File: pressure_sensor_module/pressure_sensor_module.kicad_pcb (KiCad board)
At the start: 4 copper layers, 29 x 29.5 mm, 7 parts, among them J1 Conn_02x04_Odd_Even, J2 Conn_02x07_Odd_Even, U1 MPX5100AP

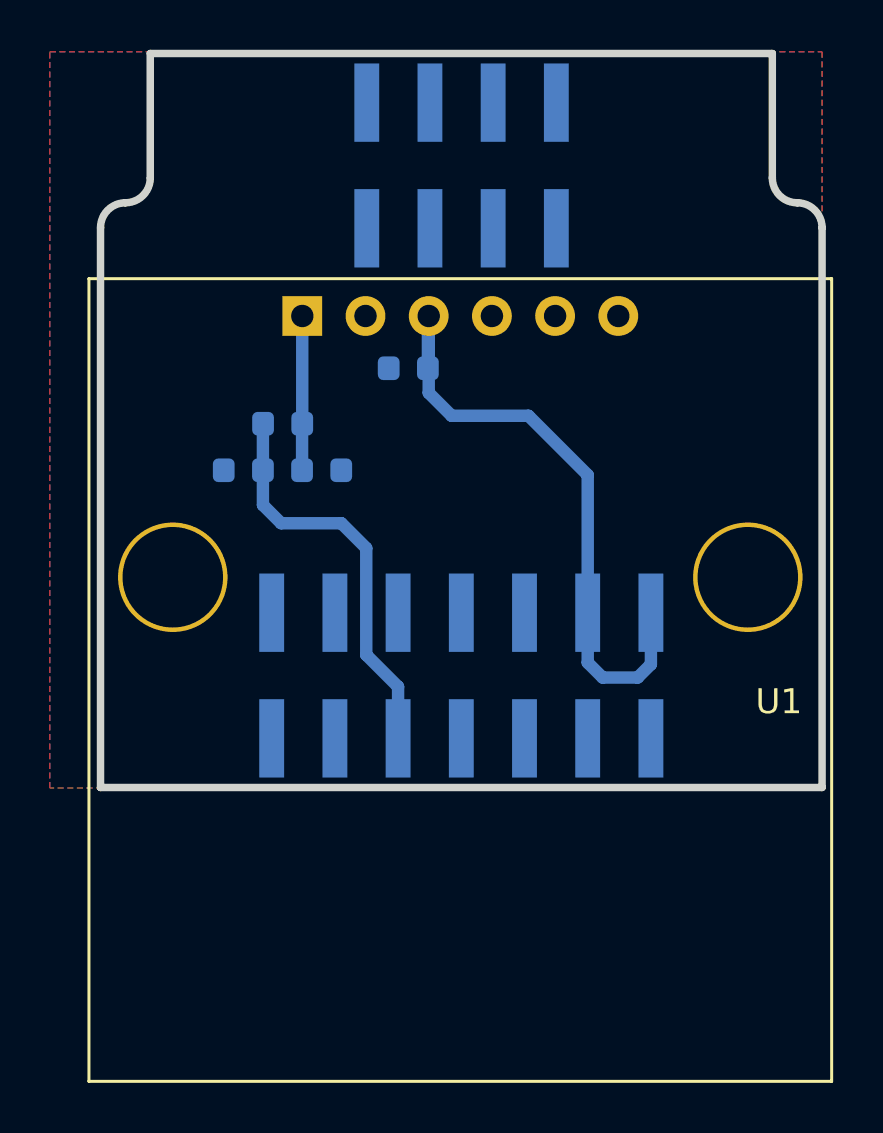
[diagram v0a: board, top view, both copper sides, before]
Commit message: added an LM358 to improve possible problems with impedance between the sensor and the STM
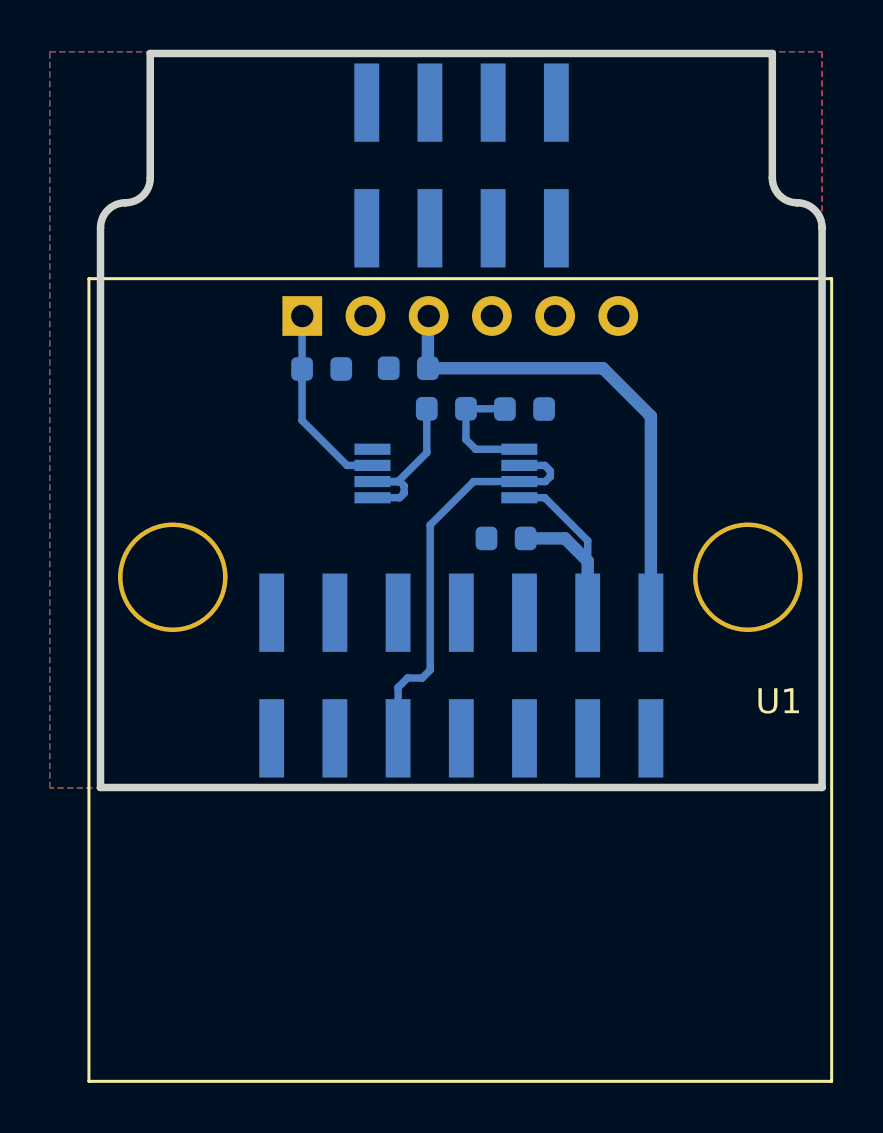
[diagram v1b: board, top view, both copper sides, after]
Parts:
- added C3: 1u, Capacitor_SMD:C_0603_1608Metric, B.Cu at (114.8, 49.6)
- added U2: LM358, Package_SO:TSSOP-8_4.4x3mm_P0.65mm, B.Cu at (112.3, 47.0)
- moved R2 11.6 mm to (115.5, 44.4), turned to 0 degrees
- moved R1 6.61 mm to (112.3, 44.4), turned to 180 degrees
- moved C2 4.07 mm to (107.3, 42.8)
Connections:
- R1 pad 1: /Analog -> Net-(R1-Pad1)
- R1 pad 2: Net-(C2-Pad1) -> Net-(R1-Pad2)
- R2 pad 1: /Analog -> Net-(R1-Pad1)
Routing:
- net Net-(R1-Pad2): track 0.00 -> 7.42 mm
- net +5V: track 25.6 -> 31.1 mm
- net Net-(R1-Pad1): track 0.00 -> 5.11 mm
- net Net-(C2-Pad1): track 6.20 -> 7.78 mm

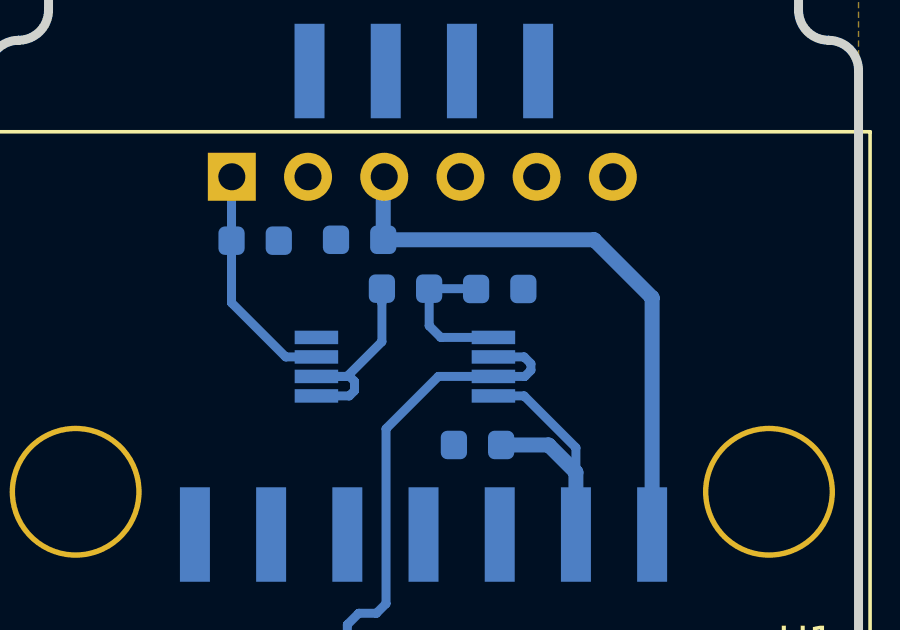
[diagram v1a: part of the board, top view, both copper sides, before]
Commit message: Added all references on silkscreen added BOM for sensor modules
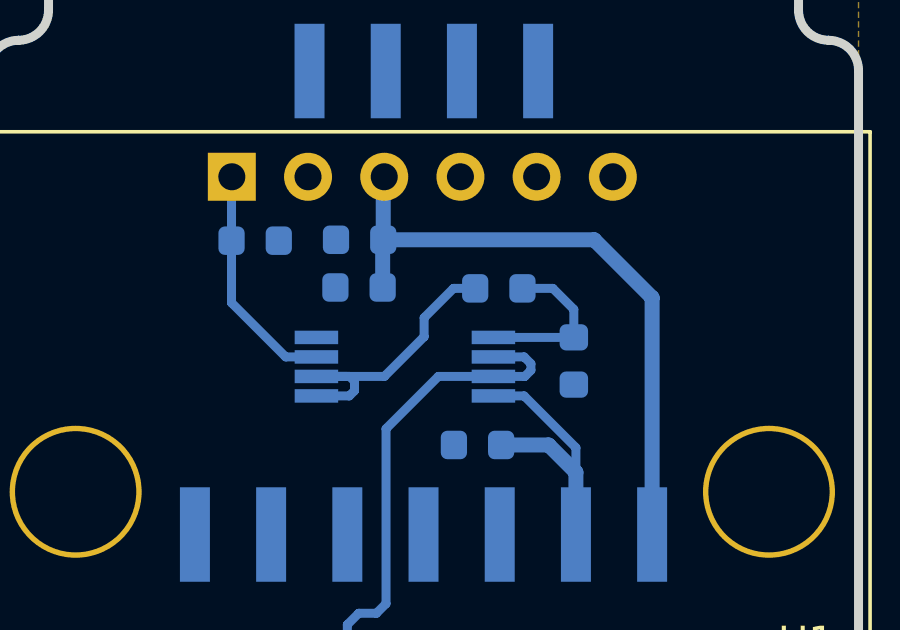
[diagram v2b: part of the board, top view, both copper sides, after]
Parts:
- added C4: 0.1u, Capacitor_SMD:C_0603_1608Metric, B.Cu at (110.8, 44.3)
- C3: value 1u -> 0.1u
- moved R2 3.44 mm to (118.0, 46.8), turned to 270 degrees
- moved R1 3.11 mm to (115.5, 44.4)
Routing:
- net Net-(R1-Pad2): track 7.42 -> 10.9 mm
- net +5V: track 31.1 -> 32.7 mm
- net Net-(R1-Pad1): track 5.11 -> 5.62 mm

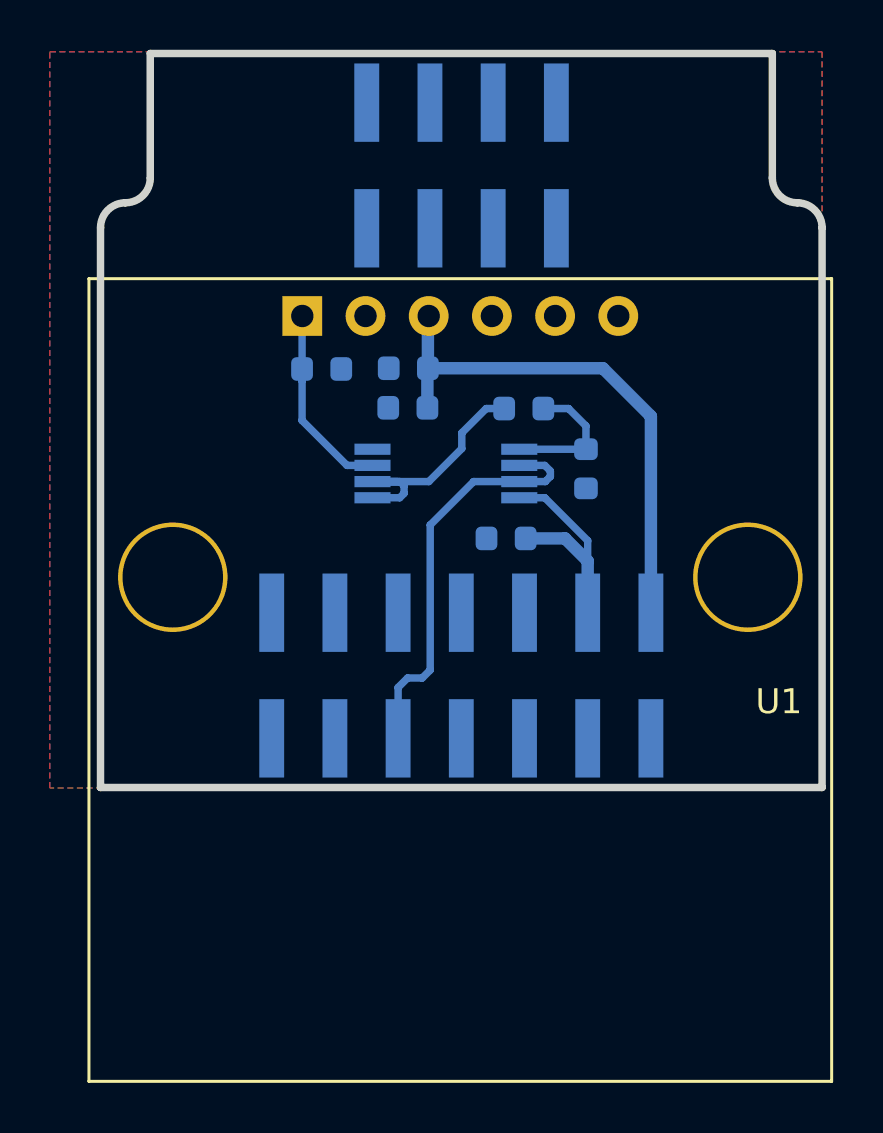
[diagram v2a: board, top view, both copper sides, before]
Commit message: J2 connector modified
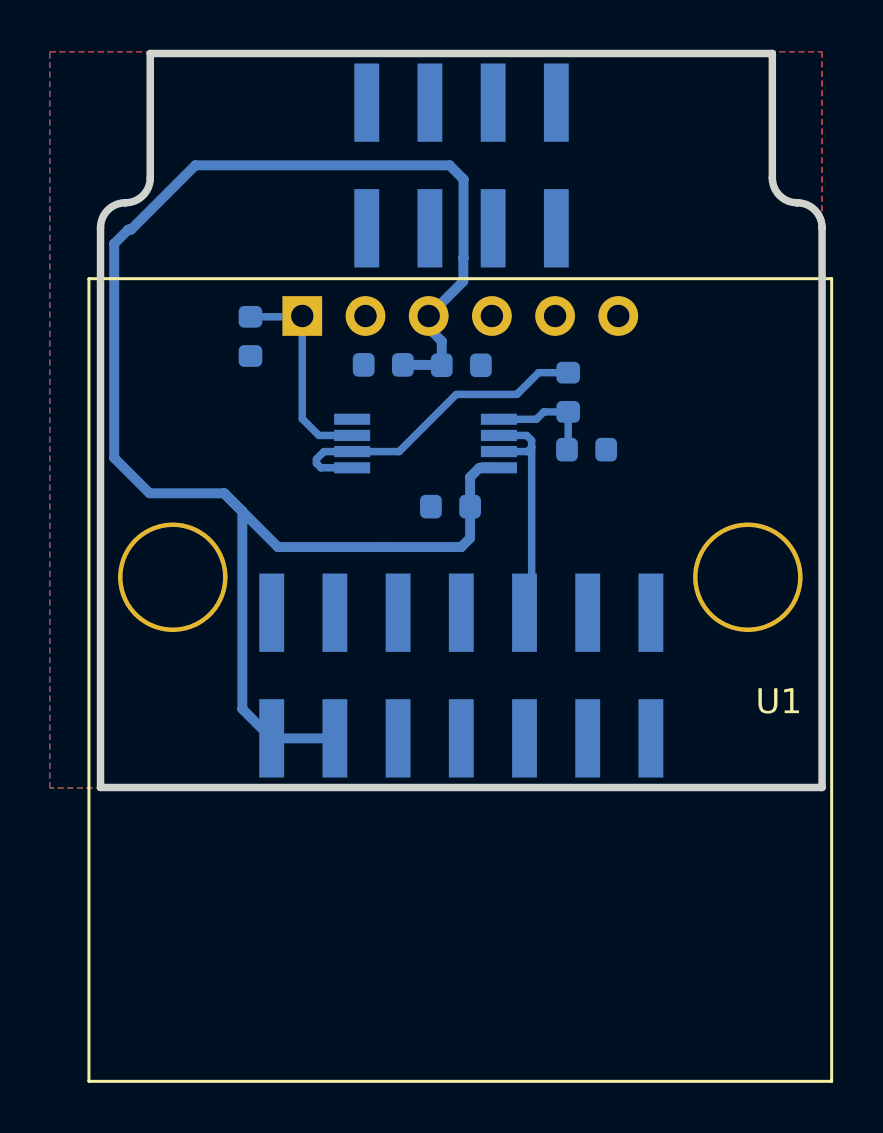
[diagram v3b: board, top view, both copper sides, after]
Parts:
- moved C2 3.15 mm to (104.5, 41.5), turned to 270 degrees
- moved C4 2.75 mm to (113.0, 42.6), turned to 0 degrees
- moved C3 2.57 mm to (112.5, 48.3)
- moved R1 1.90 mm to (117.2, 43.7), turned to 90 degrees
- moved U2 1.46 mm to (111.5, 45.8)
- moved C1 1.01 mm to (109.8, 42.6)
- moved R2 0.77 mm to (118.0, 46.0), turned to 0 degrees
- turned J2 to 270 degrees
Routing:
- net +5V: track 32.7 -> 66.9 mm
- net /Analog: track 16.7 -> 9.83 mm
- net Net-(R1-Pad2): track 10.9 -> 13.2 mm
- net /SPI_CS: track 1.20 -> 0.00 mm
- net Net-(R1-Pad1): track 5.62 -> 4.44 mm
- net Net-(C2-Pad1): track 7.78 -> 8.51 mm
